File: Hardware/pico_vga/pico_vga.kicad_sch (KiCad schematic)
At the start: 24 parts, among them J1 Conn_01x40, J2 DB15_Female_HighDensity_Mount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, U1 74HC00, U2 SN74AVC8T245PW, U3 Pico, U4 SN74AVC8T245PW

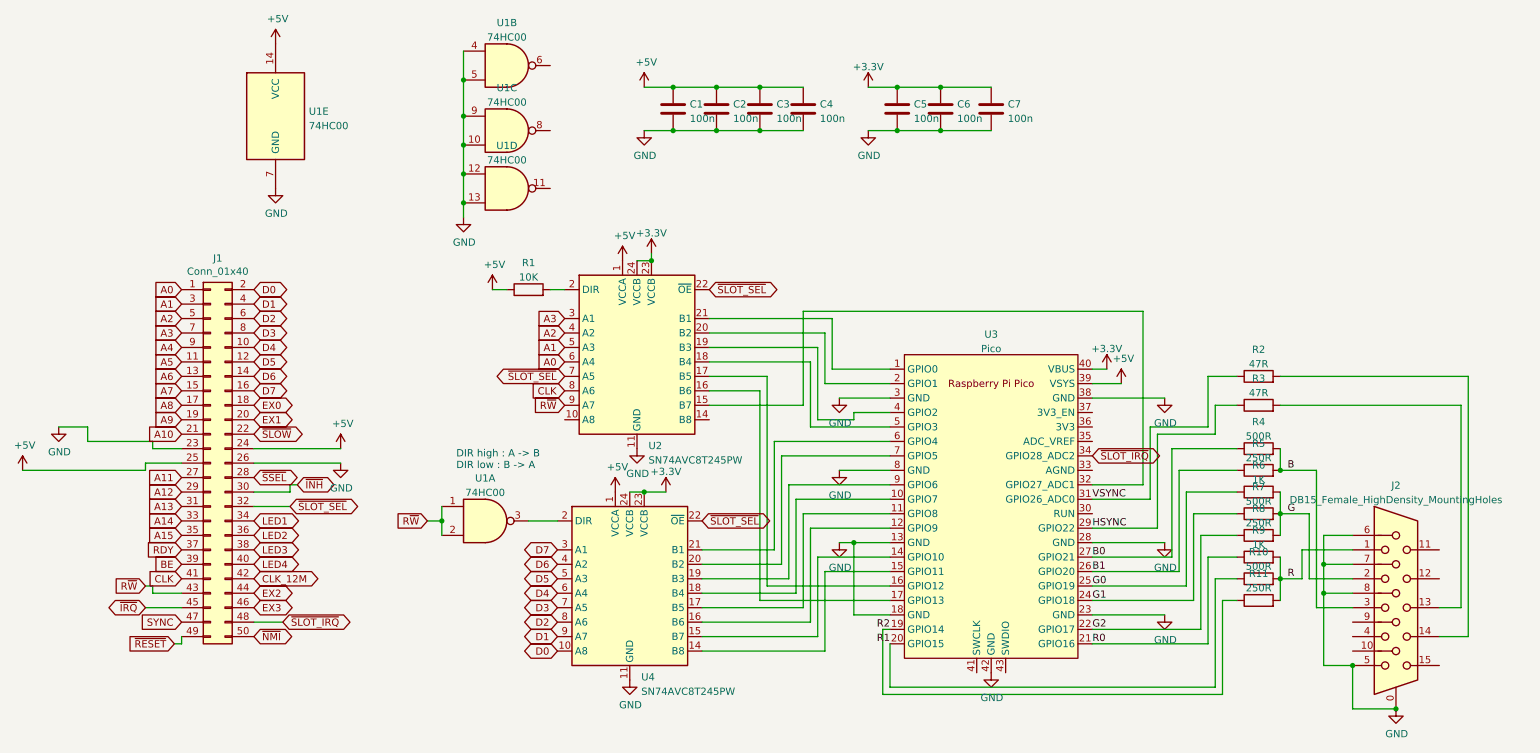
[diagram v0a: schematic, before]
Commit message: Add RAM board + some VGA things
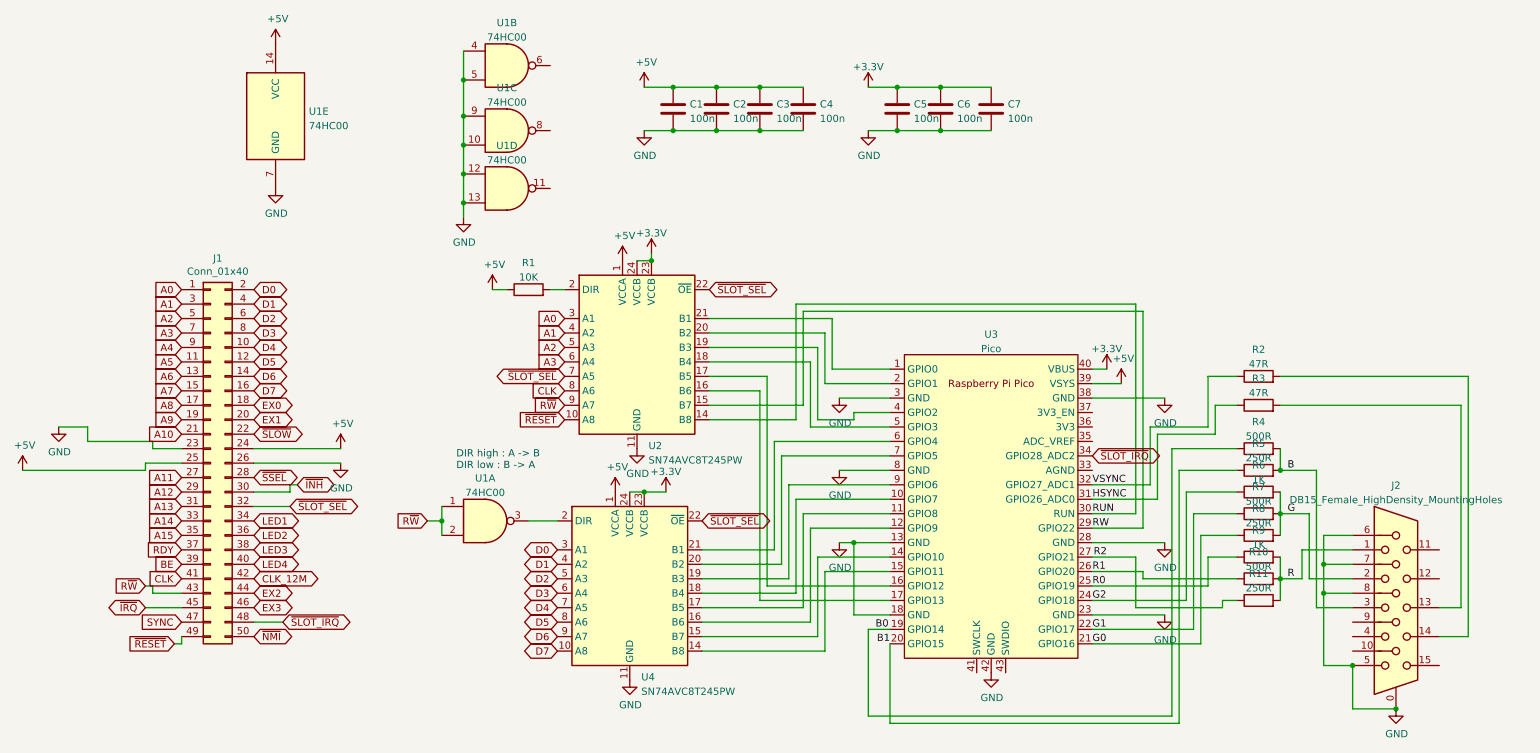
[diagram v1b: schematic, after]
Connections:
- net A0: now also U2.3 (A1); no longer U2.6 (A4)
- net A1: now also U2.4 (A2); no longer U2.5 (A3)
- net A2: now also U2.5 (A3); no longer U2.4 (A2)
- net A3: now also U2.6 (A4); no longer U2.3 (A1)
- net B0: now also U3.19 (GPIO14); no longer U3.27 (GPIO21)
- net B1: now also U3.20 (GPIO15); no longer U3.26 (GPIO20)
- net D0: now also U4.3 (A1); no longer U4.10 (A8)
- net D1: now also U4.4 (A2); no longer U4.9 (A7)
- net D2: now also U4.5 (A3); no longer U4.8 (A6)
- net D3: now also U4.6 (A4); no longer U4.7 (A5)
- net D4: now also U4.7 (A5); no longer U4.6 (A4)
- net D5: now also U4.8 (A6); no longer U4.5 (A3)
- net D6: now also U4.9 (A7); no longer U4.4 (A2)
- net D7: now also U4.10 (A8); no longer U4.3 (A1)
- net G0: now also R8.1, U3.21 (GPIO16); no longer R6.1, U3.25 (GPIO19)
- net G1: now also U3.22 (GPIO17); no longer U3.24 (GPIO18)
- net G2: now also R6.1, U3.24 (GPIO18); no longer R8.1, U3.22 (GPIO17)
- net HSYNC: now also U3.31 (GPIO26_ADC0); no longer U3.29 (GPIO22)
- net R0: now also U3.25 (GPIO19); no longer U3.21 (GPIO16)
- net R1: now also U3.26 (GPIO20); no longer U3.20 (GPIO15)
- net R2: now also U3.27 (GPIO21); no longer U3.19 (GPIO14)
- net VSYNC: now also U3.32 (GPIO27_ADC1); no longer U3.31 (GPIO26_ADC0)
- net ~{RESET}: now also U2.10 (A8)
- net RUN: now reaches U2.14 (B8)
- net RUN: now also U3.30 (RUN)
- net RW: now reaches U2.15 (B7)
- net RW: now also U3.29 (GPIO22); no longer U3.32 (GPIO27_ADC1)
